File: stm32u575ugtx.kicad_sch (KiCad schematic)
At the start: 5 parts, among them J5 TC2070, U12 STM32U575RGTx, U13 MCP2562-H-SN

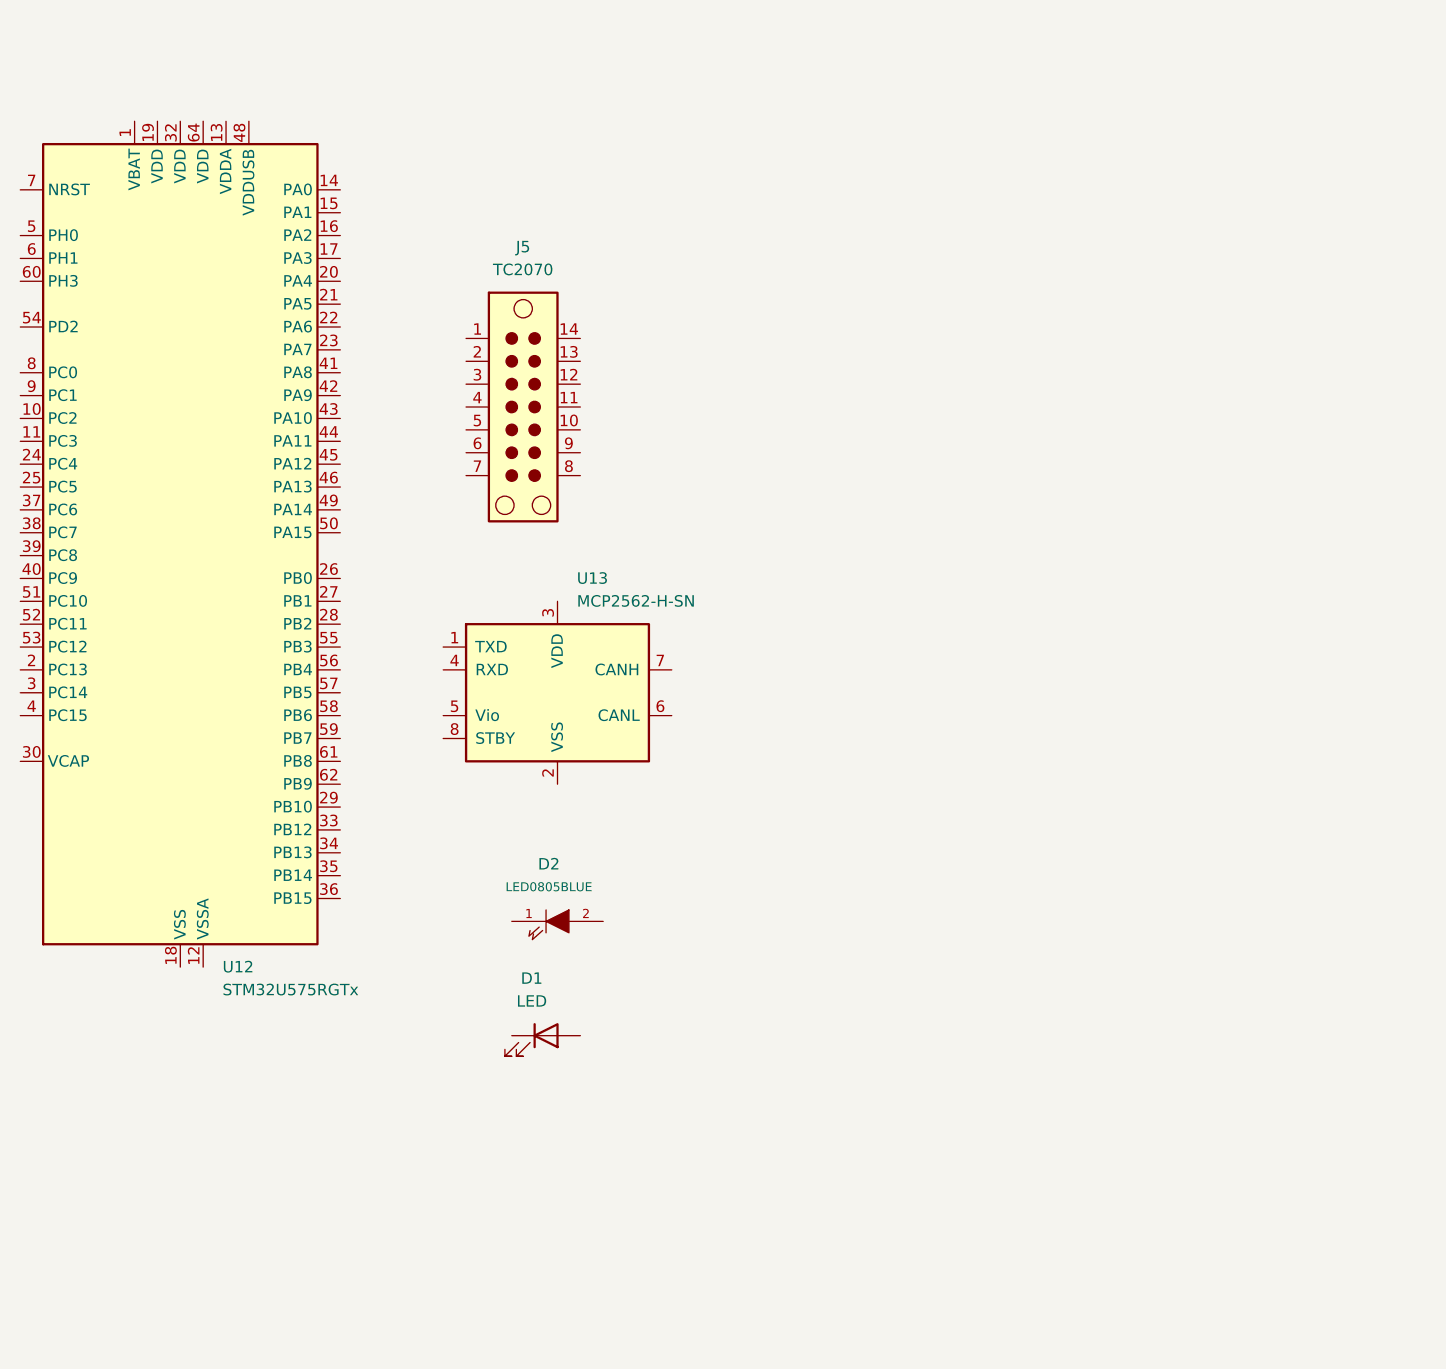
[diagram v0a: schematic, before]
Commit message: PCB 3mm free space around edges, 9pin dipswitch, re-arragnged components
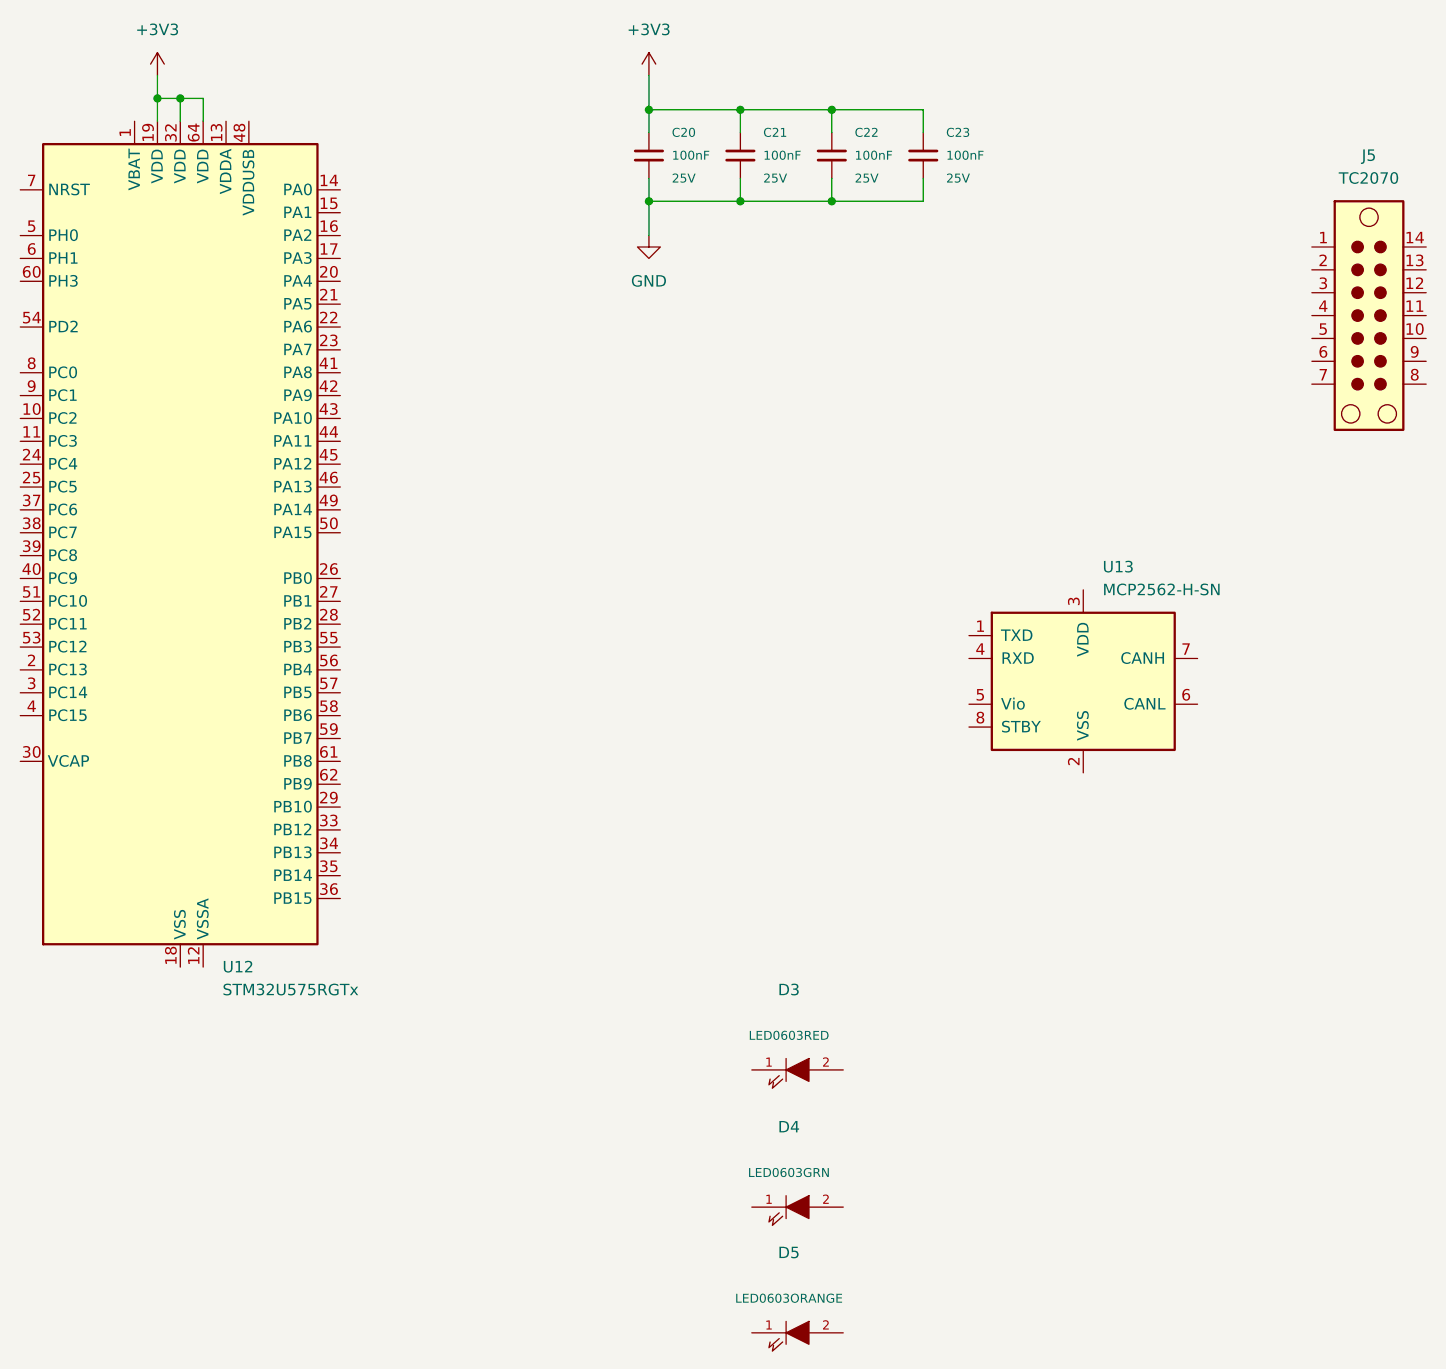
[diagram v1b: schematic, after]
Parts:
- removed D1: LED, LED_SMD:LED_0603_1608Metric, symbol Device:LED
- removed D2: LED0805BLUE#0805LED, D&R_Discrete:LED_0805, symbol D&R_Discrete:LED0805BLUE#0805LED
- added C20, C21, C22, C23: 100N-X7R_25V#0402, D&R_Passive:C_0402, symbol D&R_Passive:100N-X7R_25V#0402
- added D3: LED0603RED_APT1608EC, D&R_Discrete:LED_0603_1608Metric, symbol Doggen:LED0603RED_APT1608EC
- added D4: LED0603GRN_APT1608ZGC, D&R_Discrete:LED_0603_1608Metric, symbol Doggen:LED0603GRN_APT1608ZGC
- added D5: LED0603ORANGE_APT1608SECK, D&R_Discrete:LED_0603_1608Metric, symbol Doggen:LED0603ORANGE_APT1608SECK
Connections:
- net +3V3: now reaches U12.19 (VDD)
- net +3V3: now also U12.32 (VDD), U12.64 (VDD), C20.1, C21.1, C22.1, C23.1
- new net GND: C20.2, C21.2, C22.2, C23.2
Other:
- moved on the sheet: J5, U13

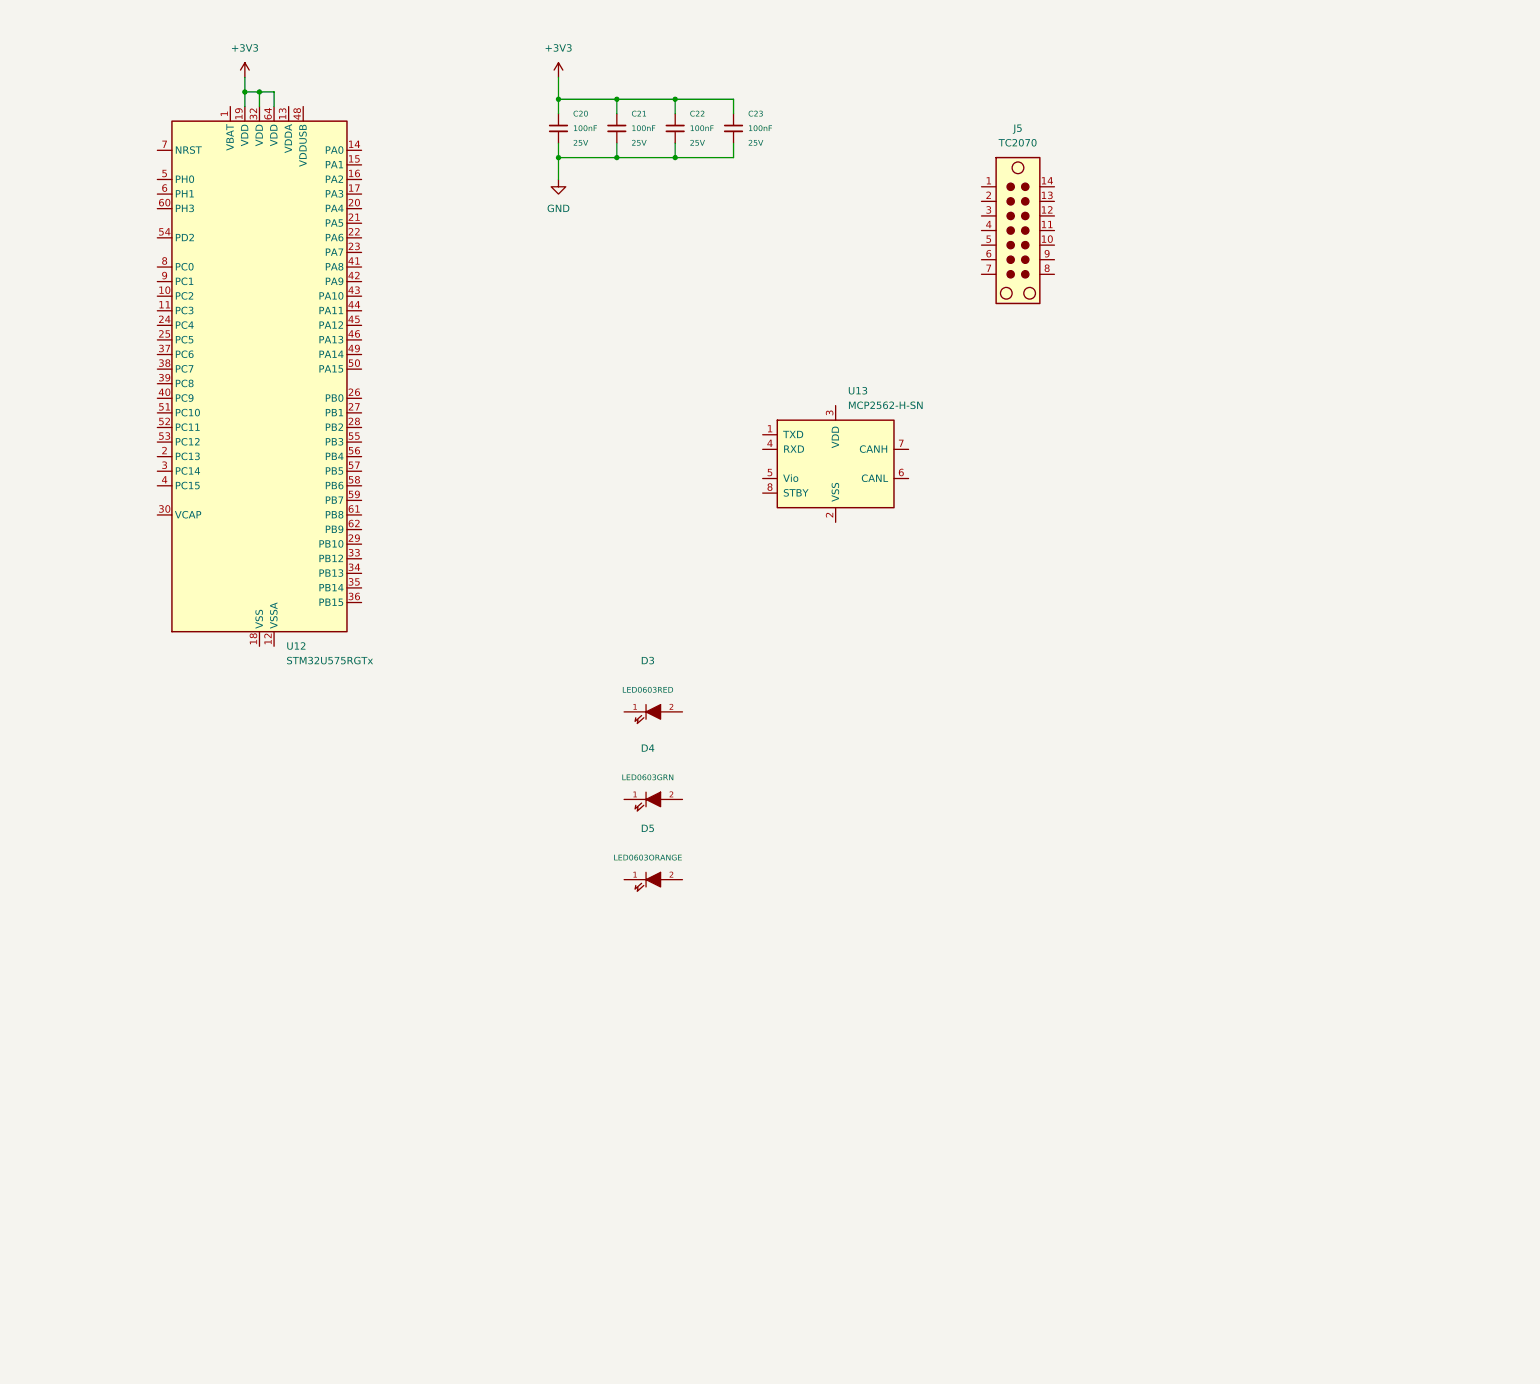
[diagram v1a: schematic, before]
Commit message: updated hierarchical sheets
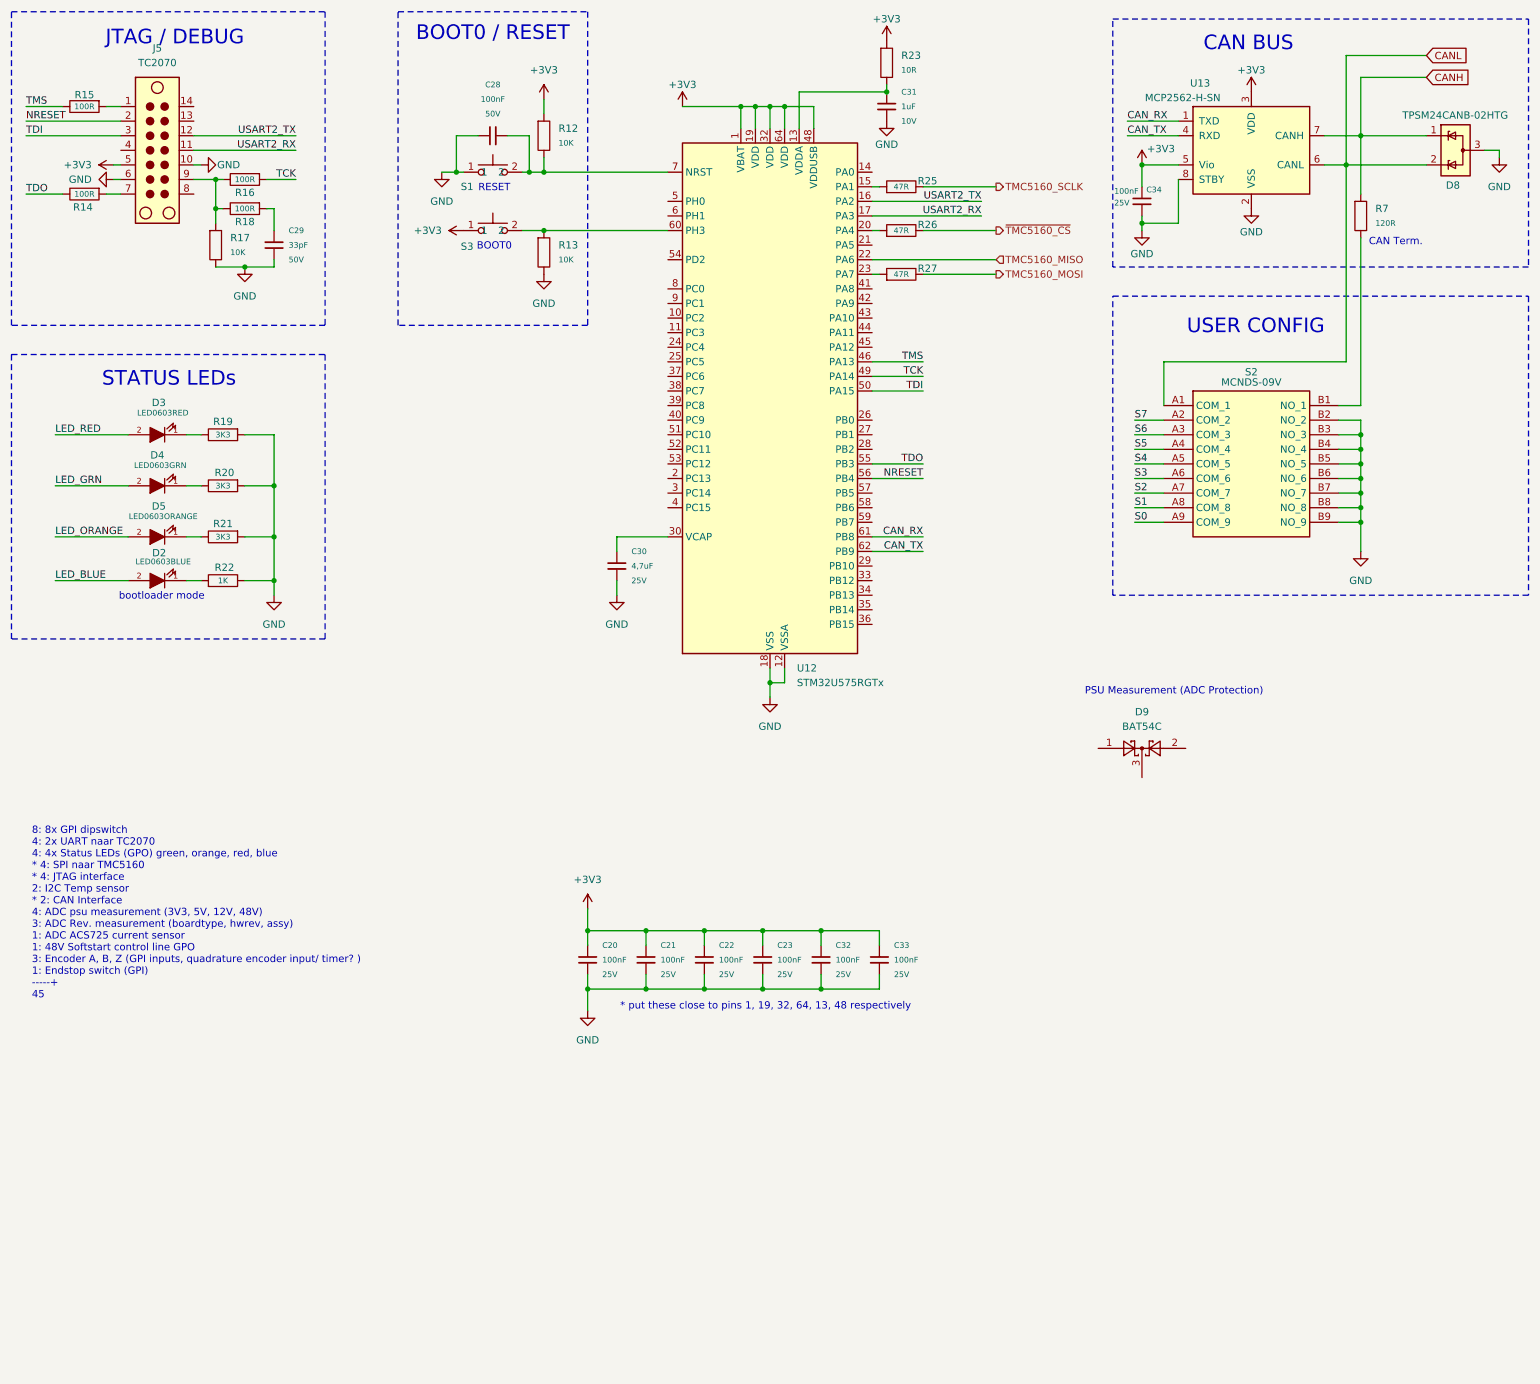
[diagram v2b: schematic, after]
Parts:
- added C28: 100N-X7R_50V#0603, D&R_Passive:C_0603, symbol D&R_Passive:100N-X7R_50V#0603
- added C29: 33P-NP0_50V#0603, D&R_Passive:C_0603, symbol Doggen:33P-NP0_50V#0603
- added C30: 4U7-X7R_25V#1206, D&R_Passive:C_1206, symbol D&R_Passive:4U7-X7R_25V#1206
- added C31: 1U-X7R_10V#0805, D&R_Passive:C_0805, symbol D&R_Passive:1U-X7R_10V#0805
- added C32, C33, C34: 100N-X7R_25V#0402, D&R_Passive:C_0402, symbol D&R_Passive:100N-X7R_25V#0402
- added D2: LED0603BLUE_APT1608LVBC/D, D&R_Discrete:LED_0603_1608Metric, symbol Doggen:LED0603BLUE_APT1608LVBC/D
- added D8: TPSM24CANB-02HTG, Package_TO_SOT_SMD:SOT-23-3, symbol Doggen:TPSM24CANB-02HTG
- added D9: BAT54C, Package_TO_SOT_SMD:SOT-23, symbol Diode:BAT54C
- added R12, R13, R17: 10K#0603, D&R_Passive:R_0603, symbol D&R_Passive:10K#0603
- added R14, R15, R16, R18: 100R#0603, D&R_Passive:R_0603, symbol D&R_Passive:100R#0603
- added R19, R20, R21: 3K3#0603, D&R_Passive:R_0603, symbol D&R_Passive:3K3#0603
- added R22: 1K#0603, D&R_Passive:R_0603, symbol D&R_Passive:1K#0603
- added R23: 10R#0603, D&R_Passive:R_0603, symbol D&R_Passive:10R#0603
- added R25, R26, R27: 47R#0603, D&R_Passive:R_0603, symbol D&R_Passive:47R#0603
- added R7: 120R#0603, D&R_Passive:R_0603, symbol D&R_Passive:120R#0603
- added S1, S3: Wurth_Tactile_Switch_430182043816, Button_Switch_SMD:SW_SPST_B3S-1000, symbol Doggen:Wurth_Tactile_Switch_430182043816
- added S2: MCNDS-09V, MCNDS09V, symbol Doggen:MCNDS-09V
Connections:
- net +3V3: now also J5.5, U12.1 (VBAT), U12.48 (VDDUSB), U13.3 (VDD), U13.5 (Vio), C32.1, C33.1, C34.1, R12.1, R23.1, S3.1
- net GND: now also J5.10, J5.6, U12.12 (VSSA), U12.18 (VSS), U12.31 (VSS), U12.47 (VSS), U12.63 (VSS), U13.2 (VSS), U13.8 (STBY), C28.2, C29.2, C30.2, C31.2, C32.2, C33.2, C34.2, D8.3 (A), R13.2, R17.2, R19.1, R20.1, R21.1, R22.2, S1.1, S2.B2 (NO_2), S2.B3 (NO_3), S2.B4 (NO_4), S2.B5 (NO_5), S2.B6 (NO_6), S2.B7 (NO_7), S2.B8 (NO_8), S2.B9 (NO_9)
- net CAN_RX: now reaches U13.1 (TXD)
- net CAN_RX: now also U12.61 (PB8)
- net CAN_TX: now reaches U13.4 (RXD)
- net CAN_TX: now also U12.62 (PB9)
- net CANL: now reaches U13.6 (CANL)
- net CANL: now also D8.2 (K), S2.A1 (COM_1)
- net CANH: now reaches U13.7 (CANH)
- net CANH: now also D8.1 (K), R7.1
- net at D5.1 (K): now also R21.2
- net LED_ORANGE: now reaches D5.2 (A)
- net at U12.13 (VDDA): now also C31.1, R23.2
- net at U12.15 (PA1): now also R25.1
- net USART2_TX: now reaches U12.16 (PA2)
- net USART2_TX: now also J5.12
- net USART2_RX: now reaches U12.17 (PA3)
- net USART2_RX: now also J5.11
- net at U12.20 (PA4): now also R26.1
- net TMC5160_MISO: now reaches U12.22 (PA6)
- net at U12.23 (PA7): now also R27.1
- net at U12.30 (VCAP): now also C30.1
- net TMS: now reaches U12.46 (PA13)
- net TMS: now also R15.2
- net TCK: now reaches U12.49 (PA14)
- net TCK: now also R16.1
- net TDI: now reaches U12.50 (PA15)
- net TDI: now also J5.3
- net TDO: now reaches U12.55 (PB3)
- net TDO: now also R14.2
- net NRESET: now reaches U12.56 (PB4)
- net NRESET: now also J5.2
- net at U12.60 (PH3): now also R13.1, S3.2
- net at U12.7 (NRST): now also C28.1, R12.2, S1.2
- net at D3.1 (K): now also R19.2
- net LED_RED: now reaches D3.2 (A)
- net at J5.1: now also R15.1
- net at J5.7: now also R14.1
- net at J5.9: now also R16.2, R17.1, R18.2
- net at D4.1 (K): now also R20.2
- net LED_GRN: now reaches D4.2 (A)
- new net: D2.1 (K), R22.1
- new net: C29.1, R18.1
- new net: R7.2, S2.B1 (NO_1)
- new net LED_BLUE: D2.2 (A)
- new net S0: S2.A9 (COM_9)
- new net S1: S2.A8 (COM_8)
- new net S2: S2.A7 (COM_7)
- new net S3: S2.A6 (COM_6)
- new net S4: S2.A5 (COM_5)
- new net S5: S2.A4 (COM_4)
- new net S6: S2.A3 (COM_3)
- new net S7: S2.A2 (COM_2)
- new net TMC5160_MOSI: R27.2
- new net TMC5160_SCLK: R25.2
- new net ~{TMC5160_CS}: R26.2
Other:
- note added: "* put these close to pins 1, 19, 32, 64, 13, 48 respectively"
- note added: "8: 8x GPI dipswitch 4: 2x UART naar TC2070 4: 4x Status LEDs (GPO) green, orange, red, blue * 4: SPI naar TMC5160 * 4: JTAG interface 2: I2C Temp sensor * 2: CAN Interface 4: ADC psu measurement (3V3, 5V, 12V, 48V) 3: ADC Rev. measurement (boardtype, hwrev, assy) 1: ADC ACS725 current sensor 1: 48V Softstart control line GPO 3: Encoder A, B, Z (GPI inputs, quadrature encoder input/ timer? ) 1: En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"
- note added: "BOOT0"
- note added: "BOOT0 / RESET"
- note added: "CAN BUS"
- note added: "CAN Term."
- note added: "JTAG / DEBUG"
- note added: "PSU Measurement (ADC Protection)"
- note added: "RESET"
- note added: "STATUS LEDs"
- note added: "USER CONFIG"
- note added: "bootloader mode"
- moved on the sheet: C20, C21, C22, C23, D3, D4, D5, J5, U12, U13
